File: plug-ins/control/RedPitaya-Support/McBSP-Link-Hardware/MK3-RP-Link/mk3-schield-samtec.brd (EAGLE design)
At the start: 59.4 x 51.2 mm, 16 parts, among them U1 SN65MLVD202A, U2 SN65MLVD202A, U3 SN65MLVD202A

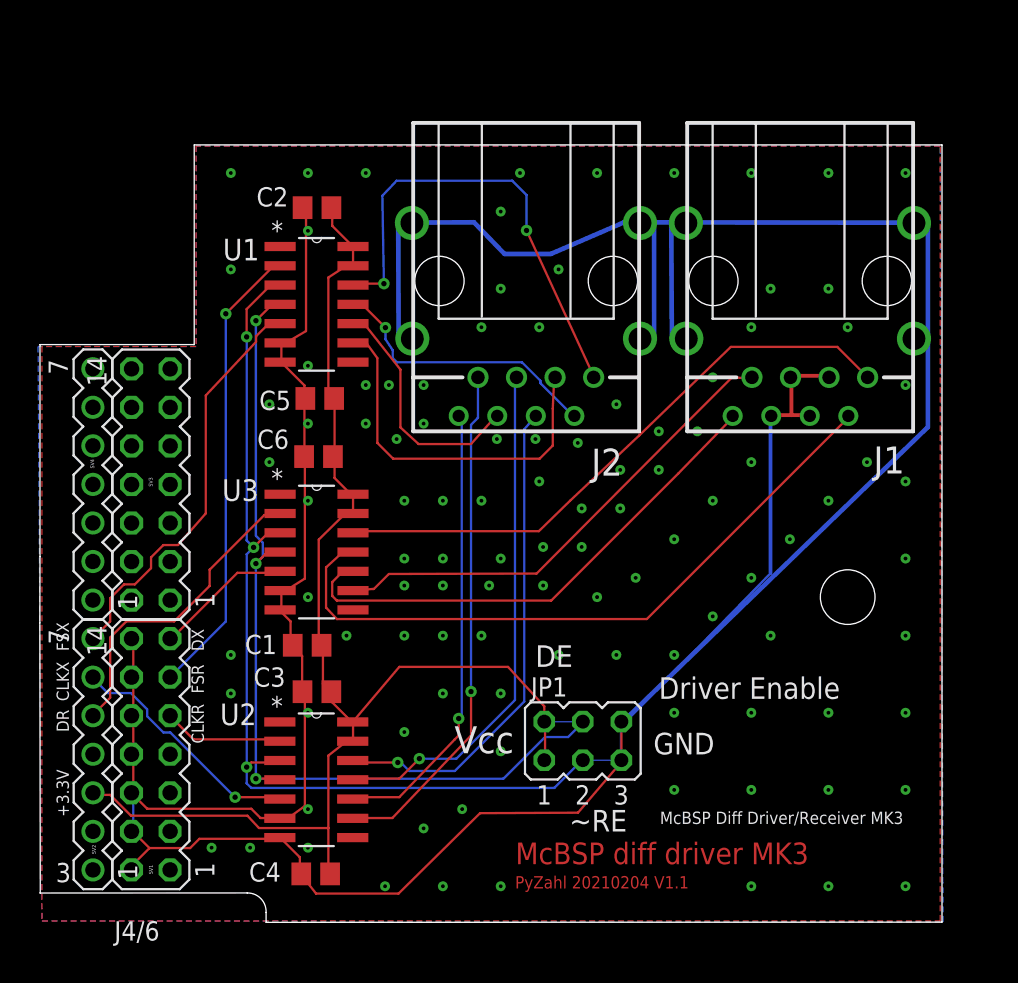
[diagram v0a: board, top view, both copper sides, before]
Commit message: added next version and support material
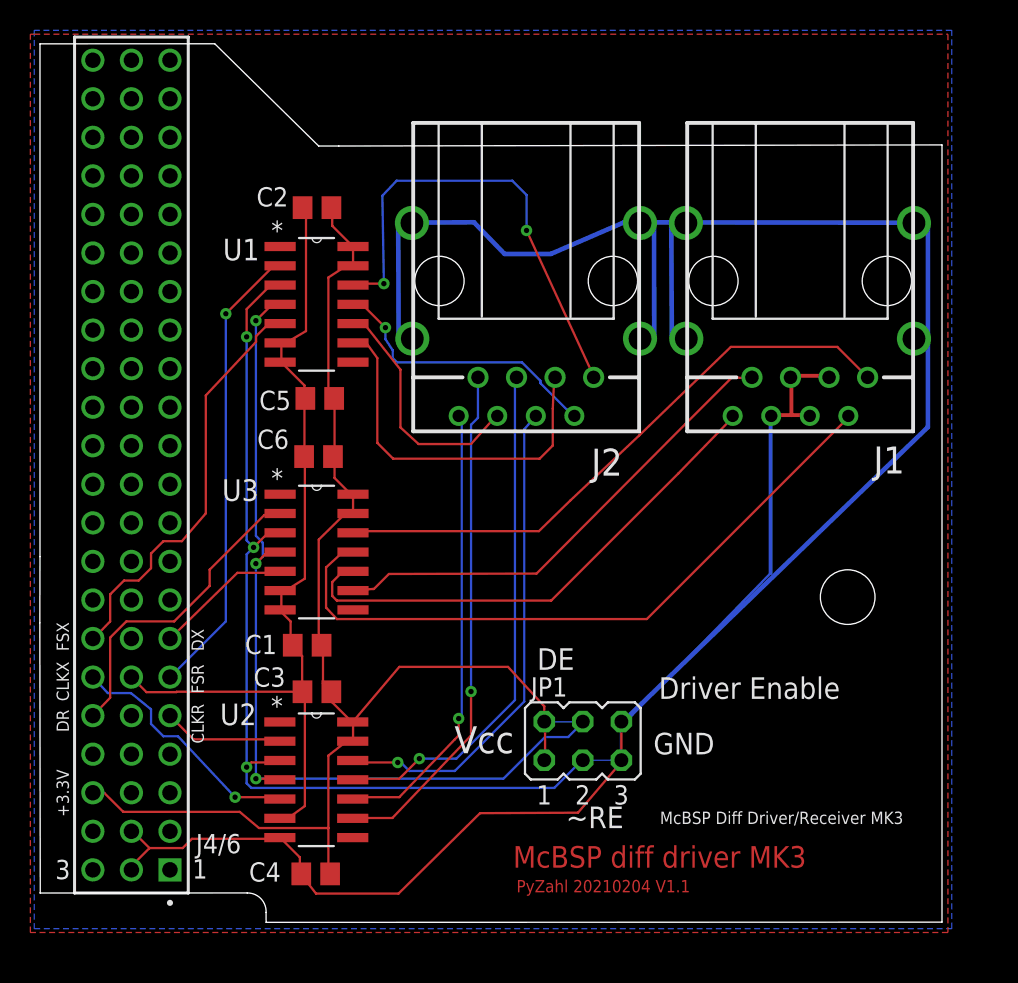
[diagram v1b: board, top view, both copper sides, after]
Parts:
- removed SV1, SV3: J4, con-lstb:MA07-2
- removed SV2, SV4: (no value), con-lstb-copy:MA07-1
- added J4/6: ESQ-122-13-L-T, ESQ-122-13-L-T:SAMTEC_ESQ-122-13-L-T
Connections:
- net CLKR0: now also J4/6.13; no longer SV1.9
- net CLKX0: now also J4/6.18; no longer SV2.6
- net DR0: now also J4/6.15; no longer SV2.5
- net DX0: now also J4/6.19; no longer SV1.13
- net FSR0: now also J4/6.16; no longer SV1.11
- net FSX0: now also J4/6.21; no longer SV2.7
- net GND: now also J4/6.02, J4/6.05, J4/6.08, J4/6.11, J4/6.14, J4/6.17, J4/6.20, J4/6.23, J4/6.26, J4/6.29, J4/6.32, J4/6.35, J4/6.38, J4/6.41, J4/6.44, J4/6.47, J4/6.50, J4/6.53, J4/6.56, J4/6.59, J4/6.62, J4/6.65; no longer SV1.10, SV1.12, SV1.14, SV1.2, SV1.4, SV1.6, SV1.8
- net VCC+3.3V: now also J4/6.09; no longer SV2.3
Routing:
- net GND: track 253.3 -> 241.0 mm
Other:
- board size 59.4 x 51.2 mm -> 59.4 x 57.9 mm
- board text added: "1"
- board text removed: "J4/6"
